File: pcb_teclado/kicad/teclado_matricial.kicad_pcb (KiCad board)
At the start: 2 copper layers, 138 x 57 mm, 31 parts

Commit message: Another Day
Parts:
- removed PinHeader: PinHeader_2x07_P2.54mm_Vertical, Connector_PinHeader_2.54mm:PinHeader_2x07_P2.54mm_Vertical
- added PinHeader_1: PinHeader_1x07_P2.54mm_Vertical, Connector_PinHeader_2.54mm:PinHeader_1x07_P2.54mm_Vertical, B.Cu at (84.7, 122.6)
- added PinHeader_2: PinHeader_1x07_P2.54mm_Vertical, Connector_PinHeader_2.54mm:PinHeader_1x07_P2.54mm_Vertical, B.Cu at (84.7, 126.1)
- renumbered Button to a, Button to b, Button to c, Button to d, Button to e, Button to enter, Button to f, Button to fun, Button to g, Button to h, Button to i, Button to j, Button to k, Button to l, Button to m, Button to n, Button to o, Button to p, Button to q, Button to r, Button to ret, Button to s, Button to space, Button to t, Button to u, Button to v, Button to w, Button to x, Button to y, Button to z
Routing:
- net .: track 2398.7 -> 2400.8 mm
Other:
- board text added: "SPACE"
- board text removed: "Shift"

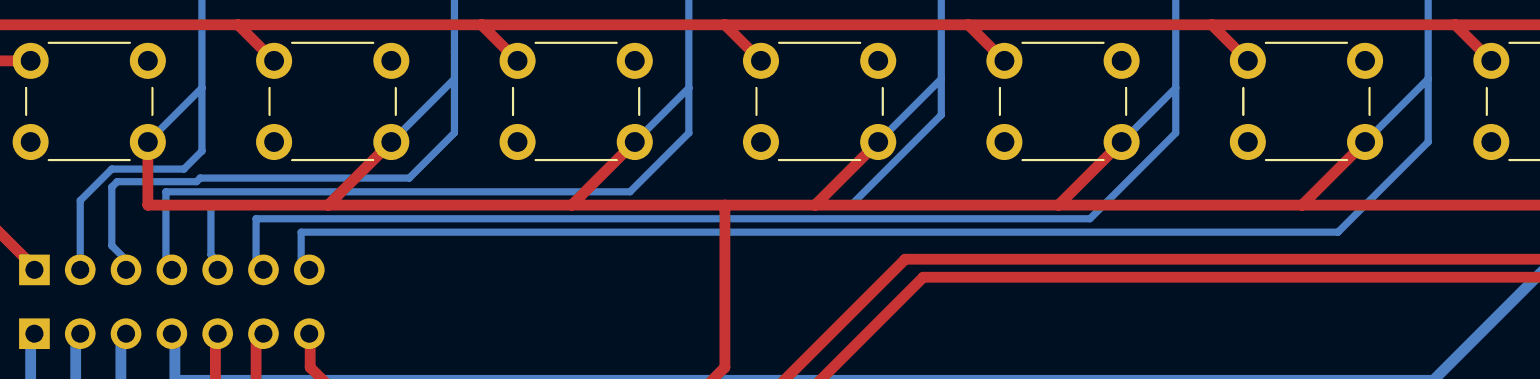
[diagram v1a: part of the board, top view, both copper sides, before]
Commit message: Added Schematic to PCB General
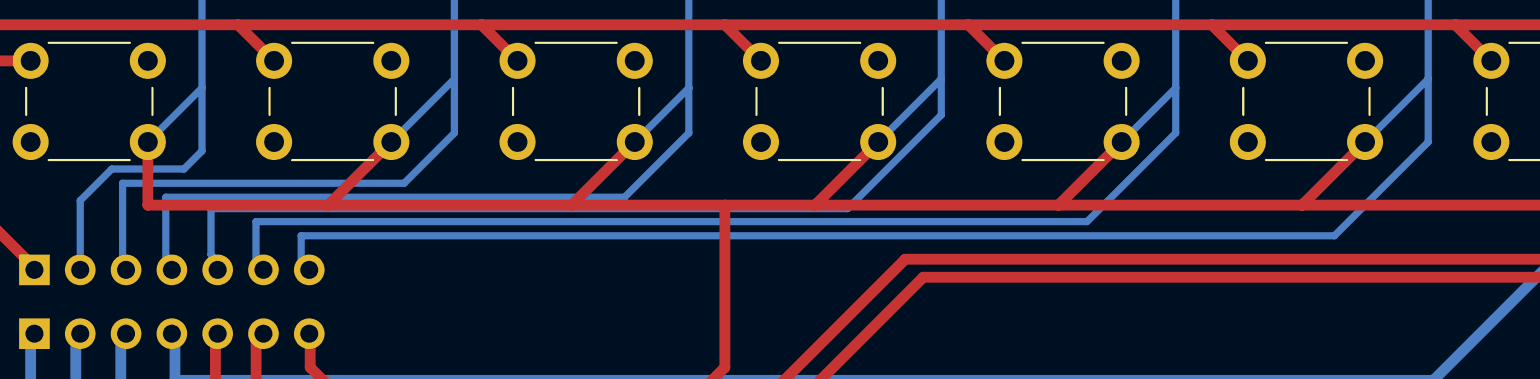
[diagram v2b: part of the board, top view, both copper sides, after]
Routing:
- net .: track 2400.8 -> 2399.6 mm
